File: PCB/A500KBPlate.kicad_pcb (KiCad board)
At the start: 2 copper layers, 448.3 x 126.5 mm, 116 parts

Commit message: Hardware finetuning, Amiga program update
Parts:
- moved LEDC11 4.80 mm to (359.1, 298.7)
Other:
- board text added: "A500KB Plate for Cherry switches Rev.3c © 2021-24 Henryk Richter"
- board text removed: "A500KB Plate for Cherry switches Rev.3b © 2021-24 Henryk Richter"
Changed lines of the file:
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@@
 	(footprint "LED_Cutout_Lib:LED_Cutout"
 		(layer "F.Cu")
-		(at 359.15 293.9)
+		(at 359.15 298.7)
 		(property "Reference" "LEDC11"
 			(at 0 -6.5 0)
@@
 		(layer "Edge.Cuts")
 	)
-	(gr_text "A500KB Plate for Cherry switches Rev.3b\n© 2021-24 Henryk Richter"
+	(gr_text "A500KB Plate for Cherry switches Rev.3c\n© 2021-24 Henryk Richter"
 		(at 359.6 356.95 0)
 		(layer "F.SilkS")

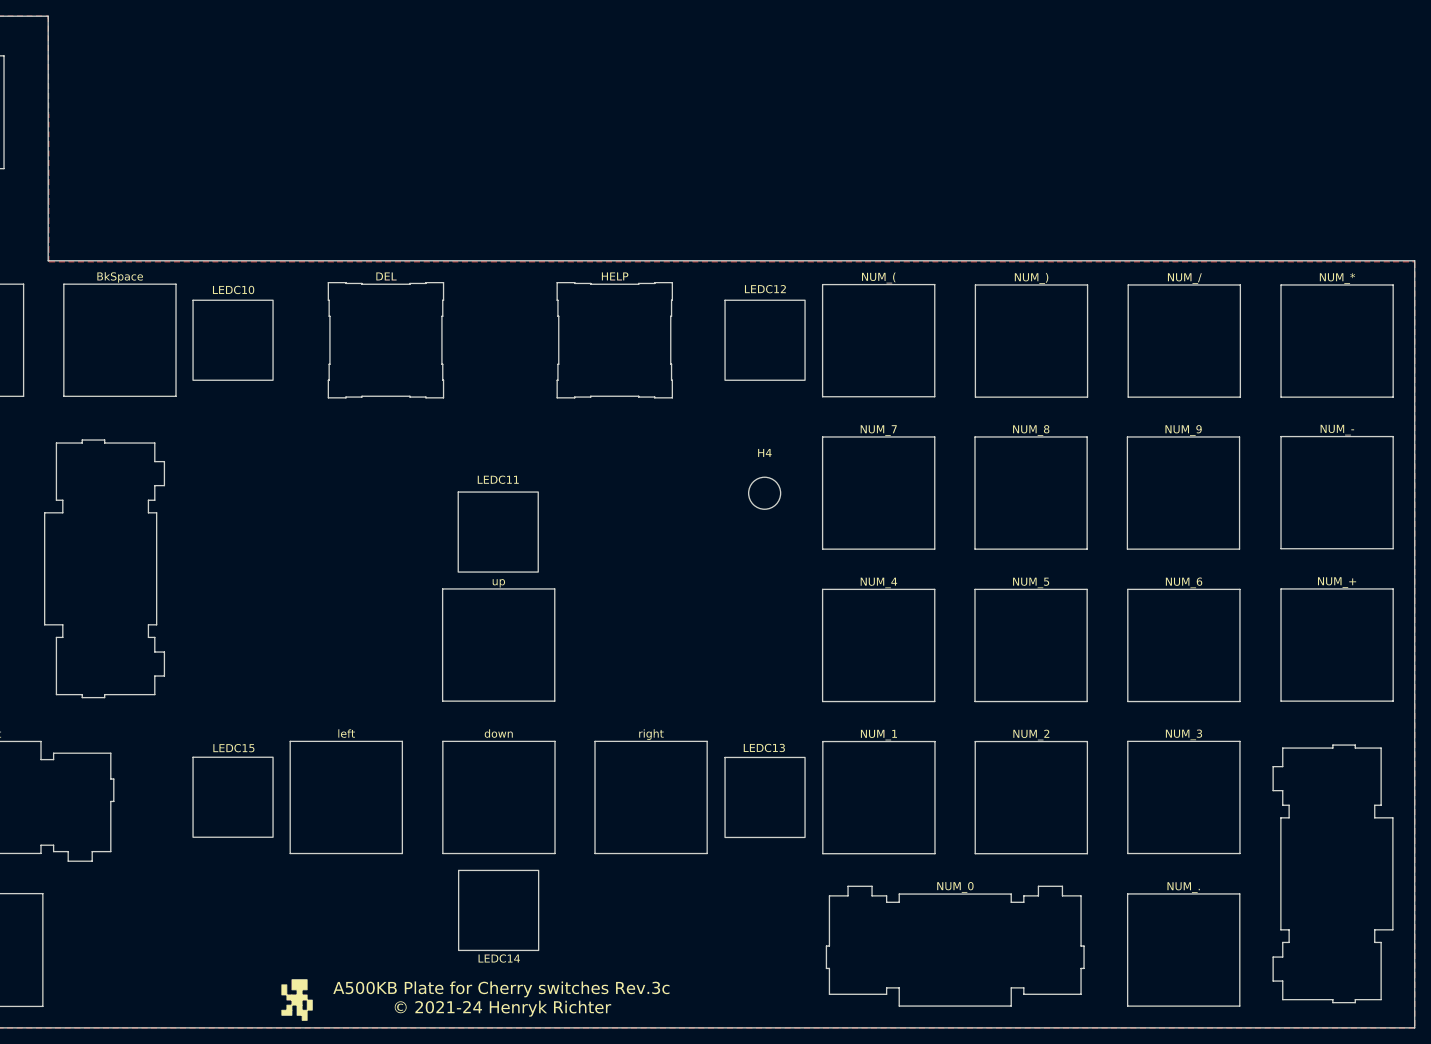
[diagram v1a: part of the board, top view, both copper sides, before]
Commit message: unified 3D printed parts for internal/external use
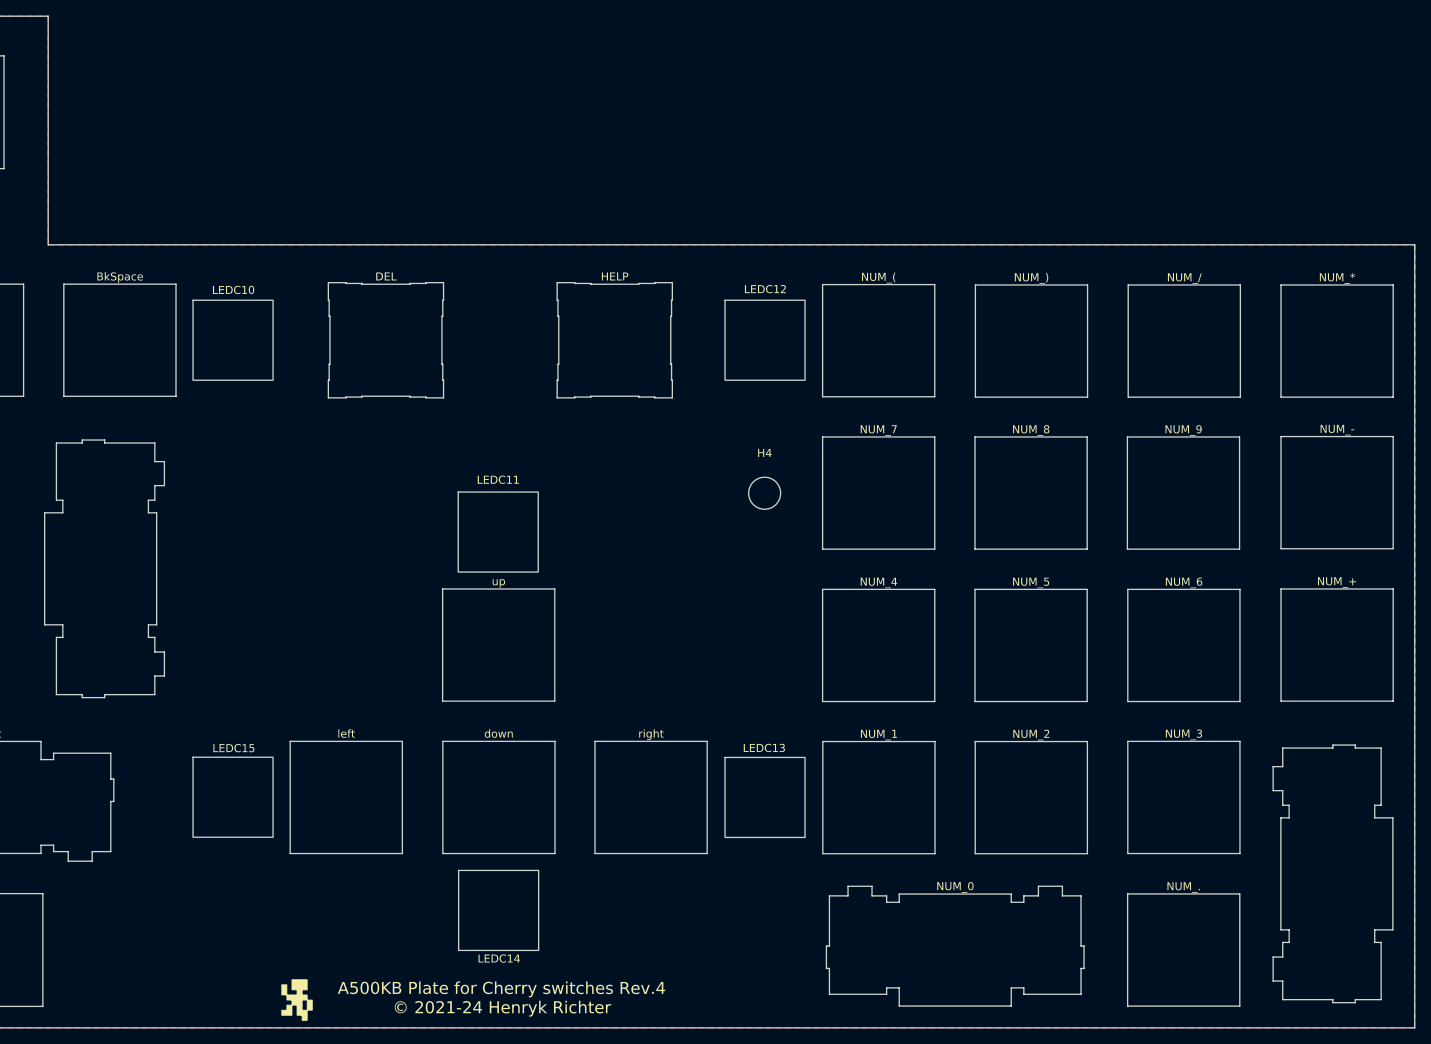
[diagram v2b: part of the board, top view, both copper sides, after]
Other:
- outline, holes or cut-outs redrawn
- board text added: "A500KB Plate for Cherry switches Rev.4 © 2021-24 Henryk Richter"
- board text removed: "A500KB Plate for Cherry switches Rev.3c © 2021-24 Henryk Richter"
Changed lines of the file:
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@@
 	)
 	(gr_line
-		(start 473.71 264.795)
+		(start 473.71 262.795)
 		(end 473.71 360.68)
 		(stroke
@@
 	)
 	(gr_line
-		(start 302.895 264.795)
-		(end 473.71 264.795)
+		(start 302.895 262.795)
+		(end 473.71 262.795)
 		(stroke
 			(width 0.05)
@@
 	(gr_line
 		(start 302.895 234.22)
-		(end 302.895 264.795)
+		(end 302.895 262.795)
 		(stroke
 			(width 0.05)
@@
 		(layer "Edge.Cuts")
 	)
-	(gr_text "A500KB Plate for Cherry switches Rev.3c\n© 2021-24 Henryk Richter"
+	(gr_text "A500KB Plate for Cherry switches Rev.4\n© 2021-24 Henryk Richter"
 		(at 359.6 356.95 0)
 		(layer "F.SilkS")
@@
 		(polygon
 			(pts
-				(xy 303.022 264.922) (xy 473.71 264.922) (xy 473.71 360.68) (xy 25.4 360.68) (xy 25.4 234.2) (xy 302.9 234.2)
-			)
-		)
+				(xy 302.9 262.8) (xy 473.75 262.8) (xy 473.71 360.68) (xy 25.4 360.68) (xy 25.4 234.2) (xy 302.9 234.2)
+			)
+		)

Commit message: added US-Only version (large Return, 2.75U LShift)
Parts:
- removed MX11: <>, MXMitsumi:MXMitsumi-1U-PlateCutout_Square
- removed MX5: LShift, MXMitsumi:MXMitsumi-1.75U-PlateCutout
- removed MX70: #, MXMitsumi:MXMitsumi-1U-PlateCutout_Square
- added MX5+11: Lshift, <>, MXMitsumi:MXMitsumi-1.75U+1U-PlateCutout, F.Cu at (52.1, 331.9)
- MX71: value Return -> Return, #; footprint MXMitsumi:MXMitsumi-ISO-PlateCutout_Cherry -> MXMitsumi:MXMitsumi-ISO+#_PlateCutout_Cherry
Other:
- board text added: "A500KB Plate for Cherry switches Rev.5 © 2021-24 Henryk Richter"
- board text added: "To swap between ISO and US layouts: - Change footprint MX5+11 from ISO version: MXMitsumi:MXMitsumi-1.75U+1U-PlateCutout to US version: MXMitsumi:MXMitsumi-2.75U-PlateCutout_Cherry - Change footprint MX71+70 from ISO version: MXMitsumi:MXMitsumi-ISO+#_PlateCutout_Cherry to US version: MXMitsumi-USReturn+Dummy_PlateCutout_Cherry (Don't forget the fills after swapping footprints: hotkey {dblquote}B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"
- board text removed: "A500KB Plate for Cherry switches Rev.4 © 2021-24 Henryk Richter"

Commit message: corrected LShift on US version plate gerbers
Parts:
- MX5+11: footprint MXMitsumi:MXMitsumi-1.75U+1U-PlateCutout -> MXMitsumi:MXMitsumi-2.75U-PlateCutout_Cherry_exact
- MX71: footprint MXMitsumi:MXMitsumi-ISO+#_PlateCutout_Cherry -> MXMitsumi:MXMitsumi-USReturn+Dummy_PlateCutout_Cherry
- turned MX5+11 to 180 degrees
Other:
- board text added: "A500KB Plate for Cherry switches Rev.5b © 2021-25 Henryk Richter"
- board text removed: "A500KB Plate for Cherry switches Rev.5 © 2021-24 Henryk Richter"
